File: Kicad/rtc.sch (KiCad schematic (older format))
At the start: 6 parts, among them U801 MCP7940N-xP, Y801 32,768 Hz

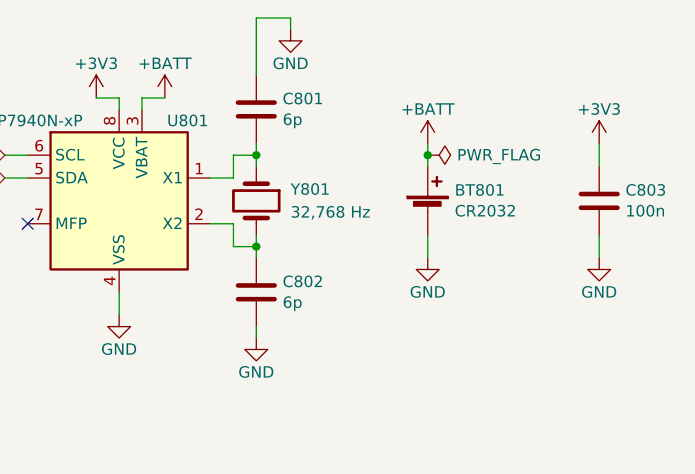
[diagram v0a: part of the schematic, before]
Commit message: Switch to 1598D enclosure.
Use MIC2005A current limiter on input.
Use soft on/off switch from Atmega.
Atmega connects to Tiva over I2C.
Use full-size SD card.
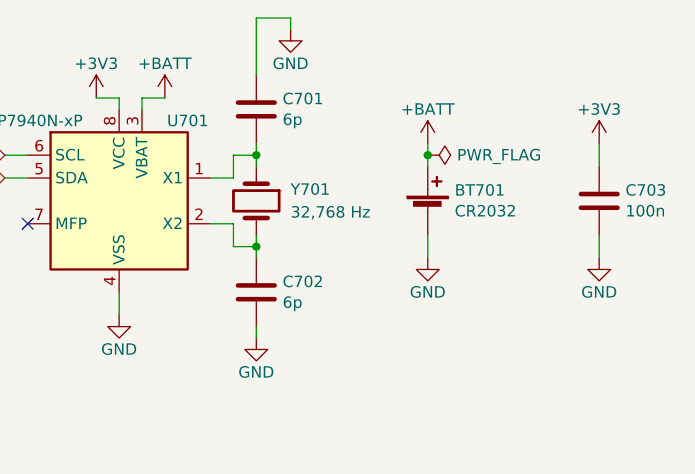
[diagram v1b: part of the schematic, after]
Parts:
- renumbered BT801 to BT701, C801 to C701, C802 to C702, C803 to C703, U801 to U701, Y801 to Y701
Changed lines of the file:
@@
 $Descr A4 11693 8268
 encoding utf-8
-Sheet 8 10
+Sheet 7 12
 Title "Neotron 32K Main PCB"
 Date "2019-12-16"
@@
 MCU_I2C_SCL
 $Comp
-L Timer:MCP7940N-xP U801
+L Timer:MCP7940N-xP U701
 U 1 1 5E0F47D7
 P 4950 3350
-F 0 "U801" H 5250 3700 50  0000 C CNN
+F 0 "U701" H 5250 3700 50  0000 C CNN
 F 1 "MCP7940N-xP" H 4550 3700 50  0000 C CNN
 F 2 "Package_DIP:DIP-8_W7.62mm" H 4950 3350 50  0001 C CNN
@@
 $EndComp
 $Comp
-L Device:Battery_Cell BT801
+L Device:Battery_Cell BT701
 U 1 1 5E0F507E
 P 6300 3400
-F 0 "BT801" H 6418 3496 50  0000 L CNN
+F 0 "BT701" H 6418 3496 50  0000 L CNN
 F 1 "CR2032" H 6418 3405 50  0000 L CNN
 F 2 "Neotron 32:BatteryHolder_Keystone_103_1x20mm" V 6300 3460 50  0001 C CNN
@@
 P 7050 3350
 AR Path="/5DF1D0B0/5E0203CB" Ref="C?"  Part="1"
-AR Path="/5DF66898/5E0203CB" Ref="C803"  Part="1"
-F 0 "C803" H 7165 3396 50  0000 L CNN
+AR Path="/5DF66898/5E0203CB" Ref="C703"  Part="1"
+F 0 "C703" H 7165 3396 50  0000 L CNN
 F 1 "100n" H 7165 3305 50  0000 L CNN
 F 2 "Capacitor_THT:C_Disc_D3.0mm_W2.0mm_P2.50mm" H 7088 3200 50  0001 C CNN
@@
 $EndComp
 $Comp
-L Device:Crystal Y801
+L Device:Crystal Y701
 U 1 1 5E028A76
 P 5550 3350
-F 0 "Y801" V 5500 3500 50  0000 L CNN
+F 0 "Y701" V 5500 3500 50  0000 L CNN
 F 1 "32,768 Hz" V 5600 3500 50  0000 L CNN
 F 2 "Crystal:Crystal_C26-LF_D2.1mm_L6.5mm_Horizontal" H 5550 3350 50  0001 C CNN
@@
 	6300 3500 6300 3600
 $Comp
-L Device:C C801
+L Device:C C701
 U 1 1 5E02C5CE
 P 5550 2950
-F 0 "C801" H 5665 2996 50  0000 L CNN
+F 0 "C701" H 5665 2996 50  0000 L CNN
 F 1 "6p" H 5665 2905 50  0000 L CNN
 F 2 "Capacitor_THT:C_Disc_D3.0mm_W2.0mm_P2.50mm" H 5588 2800 50  0001 C CNN
@@
 $EndComp
 $Comp
-L Device:C C802
+L Device:C C702
 U 1 1 5E02CC31
 P 5550 3750
-F 0 "C802" H 5665 3796 50  0000 L CNN
+F 0 "C702" H 5665 3796 50  0000 L CNN
 F 1 "6p" H 5665 3705 50  0000 L CNN
 F 2 "Capacitor_THT:C_Disc_D3.0mm_W2.0mm_P2.50mm" H 5588 3600 50  0001 C CNN
